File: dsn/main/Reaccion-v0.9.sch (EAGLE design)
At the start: 135 parts, among them J1 U.FL, Q1 2N7002K-T1-E3, Q3 2N7002K-T1-E3, Q9 SI2301CDS, T1 BC847, T2 BC847

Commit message: PCB re-design
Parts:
- removed C12: T491A336K004AT, custom_componentsv0.9:T491A336K004AT
- removed C13: EDK105M050A9BAA, custom_componentsv0.9:EDK105M050A9BAA
- removed C26, CS, CS1: 1uF, SparkFun-Capacitors:CAP0805
- removed CF1, CF2, CF3: 39pF, SparkFun-Capacitors:CAP0805
- removed D1, D2, D3: MBRS140T3-D, custom_componentsv0.9:MBRS140T3-D
- removed IC_14: MAX7313AEG, maxim:MAX7313AEG
- removed IC_2, IC_4, IC_5: LM2621, custom_componentsv0.9:LM2621
- removed JP4: GPIO, SparkFun-Connectors:M10X2
- removed JP5: POWER_JACKPTH, SparkFun-Connectors:POWER_JACKPTH
- removed L4, L5, L7: NR4018T6R8M, custom_componentsv0.9:NR4018T6R8M
- removed R29, R30, R31, R32, R33, R34, R35, R39, R40, R41, R48: 4.7K, SparkFun-Resistors:RESISTOR0805-RES
- removed RF1, RF3, RF5: 150K, SparkFun-Resistors:RESISTOR0805-RES
- removed RF2: 91K, SparkFun-Resistors:RESISTOR0805-RES
- removed RF4: 50K, SparkFun-Resistors:RESISTOR0805-RES
- removed RF6: 16K, SparkFun-Resistors:RESISTOR0805-RES
- removed RFQ, RFQ1, RFQ2: 160K, SparkFun-Resistors:RESISTOR0805-RES
- removed SJ4: SOLDERJUMPERNO, SparkFun-Retired:SOLDERJUMPERNO
- removed SJ5, SJ6: SOLDERJUMPERTRACE, SparkFun-Retired:SOLDERJUMPERTRACE
- added CIN, CIN1: 100uF, custom_componentsv0.9:TPSB107M010R0400
- added DOUT, DOUT1: SD1206S040S2R0, custom_componentsv0.9:SD1206S040S2R0
- added JP6: USB-B, SparkFun-Connectors:USBPTH
- added R13: 30K, SparkFun-Resistors:RESISTOR0805-RES
- added R14, R21: 10K, SparkFun-Resistors:RESISTOR0805-RES
- added R15: 84.5K, SparkFun-Resistors:RESISTOR0805-RES
- added U$1, U$2: LT1935ES5, custom_componentsv0.9:LT1935ES5
- added U1: MIC5219 3.3V, SparkFun-PowerIC:V_REG_MIC52193.3V
- BAT1: value (none) -> 3.7V
- C1: value T491A336K004AT -> 0.22uF; device custom_componentsv0.9:T491A336K004AT -> SparkFun-Capacitors:CAP0805
- C11: value T491A686K004AT -> 470pF; device custom_componentsv0.9:T491A686K004AT -> SparkFun-Capacitors:CAP0805
- C2: value T491A686K004AT -> 68pF; device custom_componentsv0.9:T491A686K004AT -> SparkFun-Capacitors:CAP0805
- C3: value EDK105M050A9BAA -> 22uF; device custom_componentsv0.9:EDK105M050A9BAA -> SparkFun-Capacitors:CAP0805
- C4: value T491A686K004AT -> 0.22uF; device custom_componentsv0.9:T491A686K004AT -> SparkFun-Capacitors:CAP0805
- C5: value T491A336K004AT -> 68pF; device custom_componentsv0.9:T491A336K004AT -> SparkFun-Capacitors:CAP0805
- C6: value EDK105M050A9BAA -> 47uF; device custom_componentsv0.9:EDK105M050A9BAA -> SparkFun-Capacitors:CAP0805
- L3, L6: value NR4018T6R8M -> 1.8uH; device custom_componentsv0.9:NR4018T6R8M -> inductor-bourns:SRR4028
- R1, R2: value 500 -> 10K
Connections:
- removed net 1V8_EN: IC_13.P13, IC_3.EN, R34.2
- removed net 1V8_TRANS_EN: IC_13.P14, IC_17.OE, IC_18.OE, R33.2
- removed net 2V8_TRANS_EN: IC_10.OE, IC_13.P15, R32.2
- removed net BT_RESET: IC_13.P1, IC_15.RST, R40.2
- removed net GPIO1: IC_14.P1, JP4.3
- removed net GPIO10: IC_14.P10, JP4.13
- removed net GPIO11: IC_14.P11, JP4.14
- removed net GPIO12: IC_14.P12, JP4.15
- removed net GPIO13: IC_14.P13, JP4.16
- removed net GPIO14: IC_14.P14, JP4.17
- removed net GPIO15: IC_14.P15, JP4.18
- removed net GPIO2: IC_14.P2, JP4.5
- removed net GPIO3: IC_14.P3, JP4.6
- removed net GPIO4: IC_14.P4, JP4.7
- removed net GPIO5: IC_14.P5, JP4.8
- removed net GPIO6: IC_14.P6, JP4.9
- removed net GPIO7: IC_14.P7, JP4.10
- removed net GPIO8: IC_14.P8, JP4.11
- removed net GPIO9: IC_14.P9, JP4.12
- removed net IO_INT1: IC_12.33, IC_14.!INT!/O16
- removed net N$10: CS1.2, D2.1, L7.P$2
- removed net N$16: IC_5.FREQ, RFQ2.1
- removed net N$17: CF3.1, IC_5.FB, RF5.2, RF6.1
- removed net N$40: IC_14.AD0, R29.1, SJ4.2
- removed net N$41: IC_14.AD1, R30.1, SJ5.2
- removed net N$42: IC_14.AD2, R31.1, SJ6.2
- removed net N$7: CS.2, D1.1, L4.P$2
- removed net N$9: CF2.1, IC_4.FB, RF3.2, RF4.1
- removed net W: C20.2, R18.2
- net 12V: now also C2.1, C3.1, DOUT1.C, R15.1; no longer C11.P$1, CF3.2, D3.2, RF5.1
- net 12V_EN: now also IC_12.26, R1.1; no longer IC_5.EN, R35.2
- net 3V3: now also U1.OUT; no longer C2.P$1, C26.2, CF1.2, D1.2, IC_10.VCCB, IC_14.V+, IC_17.VCCB, IC_18.VCCB, IC_3.VIN, JP1.9, JP2.1, JP4.4, R29.2, R3.2, R30.2, R31.2, R32.1, R33.1, R34.1, R35.1, R39.1, R40.1, R41.1, R48.1, R5.2, RF1.1
- net 5V: now also C5.1, C6.1, DOUT.C, IC_10.OE, IC_10.VCCB, IC_17.OE, IC_17.VCCB, IC_18.OE, IC_18.VCCB, IC_3.EN, IC_3.VIN, JP1.9, JP2.1, R13.1, R3.2, R5.2, U1.EN, U1.IN; no longer C4.P$1, C7.2, CF2.2, D2.2, IC_6.VDD, JP4.1, JP4.2, RF3.1
- net BT_CMD: now also IC_12.33, IC_15.PIO3; no longer IC_13.P2, R39.2
- net BT_EN: now also IC_12.27; no longer IC_13.P0, R41.2
- net GND: now also C1.2, C11.1, C3.2, C4.2, C6.2, CIN.-, CIN1.-, JP6.GND, R14.2, R21.2, U$1.GND, U$2.GND, U1.GND; no longer C1.P$2, C11.P$2, C12.P$2, C13.P$2, C2.P$2, C26.1, C3.P$2, C4.P$2, C5.P$2, C6.P$2, IC_14.GND, IC_2.PGND, IC_2.SGND, IC_4.PGND, IC_4.SGND, IC_5.PGND, IC_5.SGND, JP4.19, JP4.20, JP5.GND, JP5.GNDBREAK, L4.P$1, L7.P$1, RF2.2, RF4.2, RF6.2, SJ4.1, SJ5.1, SJ6.1
- net N$1: now also DOUT1.A, L3.2, U$2.SW; no longer CS.1, IC_2.SW, L3.P$2
- net N$14: now also IC_12.29; no longer D3.1, IC_5.SW, L5.P$2
- net N$2: now also DOUT.A, L6.2, U$1.SW; no longer CS1.1, IC_4.SW, L6.P$2
- net N$3: now also C1.1, R1.2, U$2.SHDN; no longer C3.P$1, IC_2.EN, IC_2.VDD, R1.1, RFQ.2
- net N$4: now also C11.2, U1.BP; no longer IC_2.FREQ, RFQ.1
- net N$5: now also C2.2, R15.2, R21.1, U$2.FB; no longer CF1.1, IC_2.FB, RF1.2, RF2.1
- net N$6: now also C5.2, R13.2, R14.1, U$1.FB; no longer C6.P$1, IC_4.EN, IC_4.VDD, R2.1, RFQ1.2
- net N$8: now also C4.1, R2.2, U$1.SHDN; no longer IC_4.FREQ, RFQ1.1
- net SCL: no longer IC_14.SLC
- net SDA: no longer IC_14.SDA
- net SIM_DATA: now also C20.2, R18.2
- net VEXT: now also C7.2, IC_6.VDD, JP6.VBUS; no longer JP5.PWR
- net VIN: now also CIN.+, CIN1.+, L3.1, L6.1, R2.1, U$1.VIN, U$2.VIN; no longer C1.P$1, C12.P$1, C13.P$1, C5.P$1, IC_2.BOOT, IC_4.BOOT, IC_5.BOOT, IC_5.VDD, L3.P$1, L5.P$1, L6.P$1, R1.2, R2.2, RFQ2.2
- net XBEE_RESET: now also IC_12.28; no longer IC_14.P0, R48.2
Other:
- moved on the sheet: C10, C27, C28, C7, C8, C9, IC_13, IC_3, IC_6, JP3, R1, R2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

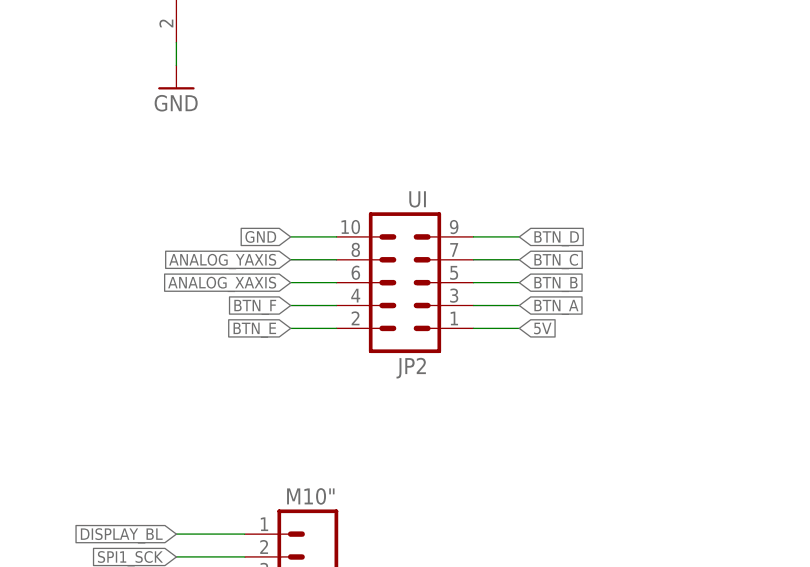
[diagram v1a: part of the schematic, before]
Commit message: Laen's DRC corrections, small modifications
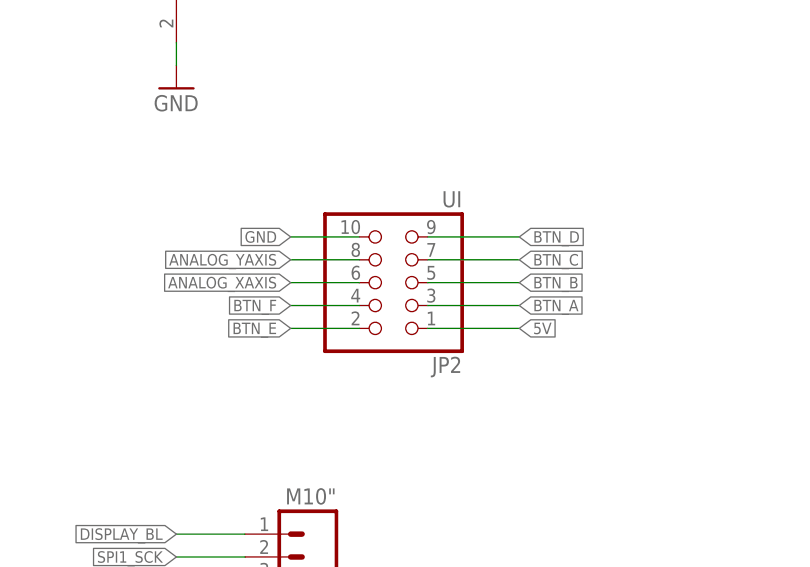
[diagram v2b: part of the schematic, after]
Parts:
- JP2: device SparkFun-Connectors:M05X2PTH -> pinhead:PINHD-2X5
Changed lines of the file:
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@@
 <setting verticaltext="up"/>
 </settings>
-<grid distance="0.01" unitdist="inch" unit="inch" style="lines" multiple="1" display="no" altdistance="0.01" altunitdist="inch" altunit="inch"/>
+<grid distance="0.1" unitdist="inch" unit="inch" style="lines" multiple="1" display="no" altdistance="0.01" altunitdist="inch" altunit="inch"/>
 <layers>
 <layer number="1" name="Top" color="4" fill="1" visible="no" active="no"/>
@@
 <part name="SJ2" library="SparkFun-Retired" deviceset="SOLDERJUMPER" device="TRACE"/>
 <part name="SJ3" library="SparkFun-Retired" deviceset="SOLDERJUMPER" device="TRACE"/>
-<part name="JP2" library="SparkFun-Connectors" deviceset="M05X2" device="PTH" value="UI"/>
+<part name="JP2" library="pinhead" deviceset="PINHD-2X5" device="" value="UI"/>
 <part name="JP3" library="SparkFun-Connectors" deviceset="M02" device="-JST-2-PTH-NO_SILK" value="BATT"/>
 <part name="BAT1" library="SparkFun-Electromechanical" deviceset="BATTERY" device="12MM" value="3.7V"/>
@@
 <instance part="SJ2" gate="1" x="162.814" y="-305.816" rot="R90"/>
 <instance part="SJ3" gate="1" x="167.894" y="-305.816" rot="R90"/>
-<instance part="JP2" gate="G$1" x="119.38" y="-353.06" rot="R180"/>
+<instance part="JP2" gate="A" x="119.38" y="-353.06" rot="R180"/>
 <instance part="JP3" gate="G$1" x="58.928" y="-11.43"/>
 <instance part="BAT1" gate="G$1" x="223.52" y="-213.36" rot="R270"/>
@@
 </segment>
 <segment>
-<pinref part="JP2" gate="G$1" pin="10"/>
-<wire x1="111.76" y1="-347.98" x2="106.68" y2="-347.98" width="0.1524" layer="91"/>
+<pinref part="JP2" gate="A" pin="10"/>
+<wire x1="114.3" y1="-347.98" x2="106.68" y2="-347.98" width="0.1524" layer="91"/>
 <label x="106.68" y="-347.98" size="1.27" layer="95" rot="R180" xref="yes"/>
 </segment>
@@
 </segment>
 <segment>
-<pinref part="JP2" gate="G$1" pin="1"/>
-<wire x1="127" y1="-358.14" x2="132.08" y2="-358.14" width="0.1524" layer="91"/>
+<pinref part="JP2" gate="A" pin="1"/>
+<wire x1="121.92" y1="-358.14" x2="132.08" y2="-358.14" width="0.1524" layer="91"/>
 <label x="132.08" y="-358.14" size="1.27" layer="95" xref="yes"/>
 </segment>
@@
 <net name="ANALOG_XAXIS" class="0">
 <segment>
-<pinref part="JP2" gate="G$1" pin="6"/>
-<wire x1="111.76" y1="-353.06" x2="106.68" y2="-353.06" width="0.1524" layer="91"/>
+<pinref part="JP2" gate="A" pin="6"/>
+<wire x1="114.3" y1="-353.06" x2="106.68" y2="-353.06" width="0.1524" layer="91"/>
 <label x="106.68" y="-353.06" size="1.27" layer="95" rot="R180" xref="yes"/>
 </segment>
@@
 <net name="ANALOG_YAXIS" class="0">
 <segment>
-<pinref part="JP2" gate="G$1" pin="8"/>
-<wire x1="111.76" y1="-350.52" x2="106.68" y2="-350.52" width="0.1524" layer="91"/>
+<pinref part="JP2" gate="A" pin="8"/>
+<wire x1="114.3" y1="-350.52" x2="106.68" y2="-350.52" width="0.1524" layer="91"/>
 <label x="106.68" y="-350.52" size="1.27" layer="95" rot="R180" xref="yes"/>
 </segment>
@@
 </segment>
 <segment>
-<pinref part="JP2" gate="G$1" pin="3"/>
-<wire x1="127" y1="-355.6" x2="132.08" y2="-355.6" width="0.1524" layer="91"/>
+<pinref part="JP2" gate="A" pin="3"/>
+<wire x1="121.92" y1="-355.6" x2="132.08" y2="-355.6" width="0.1524" layer="91"/>
 <label x="132.08" y="-355.6" size="1.27" layer="95" xref="yes"/>
 </segment>
@@
 </segment>
 <segment>
-<pinref part="JP2" gate="G$1" pin="5"/>
-<wire x1="127" y1="-353.06" x2="132.08" y2="-353.06" width="0.1524" layer="91"/>
+<pinref part="JP2" gate="A" pin="5"/>
+<wire x1="121.92" y1="-353.06" x2="132.08" y2="-353.06" width="0.1524" layer="91"/>
 <label x="132.08" y="-353.06" size="1.27" layer="95" xref="yes"/>
 </segment>
@@
 </segment>
 <segment>
-<pinref part="JP2" gate="G$1" pin="7"/>
-<wire x1="127" y1="-350.52" x2="132.08" y2="-350.52" width="0.1524" layer="91"/>
+<pinref part="JP2" gate="A" pin="7"/>
+<wire x1="121.92" y1="-350.52" x2="132.08" y2="-350.52" width="0.1524" layer="91"/>
 <label x="132.08" y="-350.52" size="1.27" layer="95" xref="yes"/>
 </segment>
@@
 </segment>
 <segment>
-<pinref part="JP2" gate="G$1" pin="9"/>
-<wire x1="127" y1="-347.98" x2="132.08" y2="-347.98" width="0.1524" layer="91"/>
+<pinref part="JP2" gate="A" pin="9"/>
+<wire x1="121.92" y1="-347.98" x2="132.08" y2="-347.98" width="0.1524" layer="91"/>
 <label x="132.08" y="-347.98" size="1.27" layer="95" xref="yes"/>
 </segment>
@@
 <net name="BTN_E" class="0">
 <segment>
-<pinref part="JP2" gate="G$1" pin="2"/>
-<wire x1="111.76" y1="-358.14" x2="106.68" y2="-358.14" width="0.1524" layer="91"/>
+<pinref part="JP2" gate="A" pin="2"/>
+<wire x1="114.3" y1="-358.14" x2="106.68" y2="-358.14" width="0.1524" layer="91"/>
 <label x="106.68" y="-358.14" size="1.27" layer="95" rot="R180" xref="yes"/>
 </segment>
@@
 <net name="BTN_F" class="0">
 <segment>
-<pinref part="JP2" gate="G$1" pin="4"/>
-<wire x1="111.76" y1="-355.6" x2="106.68" y2="-355.6" width="0.1524" layer="91"/>
+<pinref part="JP2" gate="A" pin="4"/>
+<wire x1="114.3" y1="-355.6" x2="106.68" y2="-355.6" width="0.1524" layer="91"/>
 <label x="106.68" y="-355.6" size="1.27" layer="95" rot="R180" xref="yes"/>
 </segment>

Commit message: Added power source corrections
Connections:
- removed net N$14: IC_12.29
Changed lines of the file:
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@@
 <setting verticaltext="up"/>
 </settings>
-<grid distance="0.1" unitdist="inch" unit="inch" style="lines" multiple="1" display="no" altdistance="0.01" altunitdist="inch" altunit="inch"/>
+<grid distance="0.01" unitdist="inch" unit="inch" style="lines" multiple="1" display="no" altdistance="0.01" altunitdist="inch" altunit="inch"/>
 <layers>
 <layer number="1" name="Top" color="4" fill="1" visible="no" active="no"/>
@@
 </segment>
 </net>
-<net name="N$14" class="0">
-<segment>
-<wire x1="172.72" y1="-248.92" x2="167.64" y2="-248.92" width="0.1524" layer="91"/>
-<label x="167.64" y="-248.92" size="1.27" layer="95" rot="R180" xref="yes"/>
-<pinref part="IC_12" gate="G$1" pin="29"/>
-</segment>
-</net>

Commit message: Initial release for Prototipo1
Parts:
- IC_7: device Reaccion-Custom:MMA8653FC -> Reaccion-Custom-revised:MMA8653FC
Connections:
- net BT_RX: now also IC_12.21/A7; no longer IC_12.25
- net BT_TX: now also IC_12.20/A6; no longer IC_12.24
- net CHG_STAT: now also IC_13.P1
- net DISPLAY_BL: now also IC_12.24; no longer IC_12.20/A6
- net PWR_STAT: now also IC_13.P0
- net SIM900_RESET: now also IC_12.25; no longer IC_12.21/A7
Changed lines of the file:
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@@
 <part name="GND53" library="SparkFun-Aesthetics" deviceset="GND" device=""/>
 <part name="IC_8" library="Reaccion-Custom" deviceset="MS5637-02BA03" device=""/>
-<part name="IC_7" library="Reaccion-Custom" deviceset="MMA8653FC" device=""/>
+<part name="IC_7" library="Reaccion-Custom-revised" deviceset="MMA8653FC" device=""/>
 <part name="GND35" library="SparkFun-Aesthetics" deviceset="GND" device=""/>
 <part name="GND54" library="SparkFun-Aesthetics" deviceset="GND" device=""/>
@@
 <junction x="148.336" y="-12.446"/>
 </segment>
+<segment>
+<pinref part="IC_13" gate="G$1" pin="P1"/>
+<wire x1="213.614" y1="-310.896" x2="218.694" y2="-310.896" width="0.1524" layer="91"/>
+<label x="218.948" y="-310.896" size="1.27" layer="95" xref="yes"/>
+</segment>
 </net>
 <net name="N$11" class="0">
@@
 <label x="150.876" y="-9.906" size="1.27" layer="95" xref="yes"/>
 <junction x="148.336" y="-9.906"/>
+</segment>
+<segment>
+<pinref part="IC_13" gate="G$1" pin="P0"/>
+<wire x1="213.614" y1="-313.436" x2="218.694" y2="-313.436" width="0.1524" layer="91"/>
+<label x="218.694" y="-313.436" size="1.27" layer="95" xref="yes"/>
 </segment>
 </net>
@@
 </segment>
 <segment>
-<pinref part="IC_12" gate="G$1" pin="21/A7"/>
-<wire x1="203.2" y1="-243.84" x2="208.28" y2="-243.84" width="0.1524" layer="91"/>
-<label x="208.28" y="-243.84" size="1.27" layer="95" xref="yes"/>
+<pinref part="IC_12" gate="G$1" pin="25"/>
+<wire x1="172.72" y1="-238.76" x2="167.64" y2="-238.76" width="0.1524" layer="91"/>
+<label x="167.64" y="-238.76" size="1.27" layer="95" rot="R180" xref="yes"/>
 </segment>
 </net>
@@
 </segment>
 <segment>
-<pinref part="IC_12" gate="G$1" pin="24"/>
-<wire x1="172.72" y1="-236.22" x2="167.64" y2="-236.22" width="0.1524" layer="91"/>
-<label x="167.64" y="-236.22" size="1.27" layer="95" rot="R180" xref="yes"/>
+<pinref part="IC_12" gate="G$1" pin="20/A6"/>
+<wire x1="203.2" y1="-246.38" x2="208.28" y2="-246.38" width="0.1524" layer="91"/>
+<label x="208.28" y="-246.38" size="1.27" layer="95" xref="yes"/>
 </segment>
 </net>
@@
 </segment>
 <segment>
-<pinref part="IC_12" gate="G$1" pin="25"/>
-<wire x1="172.72" y1="-238.76" x2="167.64" y2="-238.76" width="0.1524" layer="91"/>
-<label x="167.64" y="-238.76" size="1.27" layer="95" rot="R180" xref="yes"/>
+<pinref part="IC_12" gate="G$1" pin="21/A7"/>
+<wire x1="203.2" y1="-243.84" x2="208.28" y2="-243.84" width="0.1524" layer="91"/>
+<label x="208.28" y="-243.84" size="1.27" layer="95" xref="yes"/>
 </segment>
 </net>
@@
 </segment>
 <segment>
-<pinref part="IC_12" gate="G$1" pin="20/A6"/>
-<wire x1="203.2" y1="-246.38" x2="208.28" y2="-246.38" width="0.1524" layer="91"/>
-<label x="208.28" y="-246.38" size="1.27" layer="95" xref="yes"/>
-</segment>
-</net>
+<pinref part="IC_12" gate="G$1" pin="24"/>
+<wire x1="172.72" y1="-236.22" x2="167.64" y2="-236.22" width="0.1524" layer="91"/>
+<label x="167.64" y="-236.22" size="1.27" layer="95" rot="R180" xref="yes"/>
+</segment>
+</net>
